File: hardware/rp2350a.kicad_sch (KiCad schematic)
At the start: 46 parts, among them Q2 DMN1150UFB-7B, Q3 DMN1150UFB-7B, U10 RP2354A, U11 TS2306A 240GF MSM 9_C2976675, X1 XTM25012000JT00351001

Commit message: piu1
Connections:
- net PIOUART0_RX: now also U10.5 (GPIO3); no longer U10.13 (GPIO9)
- net PIOUART0_TX: now also U10.4 (GPIO2); no longer U10.12 (GPIO8)
- net UART1_RX: now also U10.13 (GPIO9); no longer U10.5 (GPIO3)
- net UART1_TX: now also U10.12 (GPIO8); no longer U10.4 (GPIO2)
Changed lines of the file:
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@@
+		)
+	)
+	(hierarchical_label "UART1_TX"
+		(shape output)
+		(at 321.31 219.71 0)
+		(effects
+			(font
+				(size 1.27 1.27)
+			)
+			(justify left)
 		)
 	)
@@
 		)
 	)
-	(hierarchical_label "UART1_TX"
-		(shape output)
-		(at 321.31 226.06 0)
+	(hierarchical_label "PIOUART0_RX"
+		(shape input)
+		(at 321.31 228.6 0)
 		(effects
 			(font
@@
 		(shape output)
 		(at 321.31 264.16 0)
-		(effects
-			(font
-				(size 1.27 1.27)
-			)
-			(justify left)
-		)
-	)
-	(hierarchical_label "PIOUART0_RX"
-		(shape input)
-		(at 321.31 222.25 0)
 		(effects
 			(font
@@
 		)
 	)
-	(hierarchical_label "UART1_RX"
+	(hierarchical_label "UART0_RX"
 		(shape input)
-		(at 321.31 228.6 0)
+		(at 321.31 215.9 0)
 		(effects
 			(font
@@
 		)
 	)
-	(hierarchical_label "UART0_RX"
+	(hierarchical_label "UART1_RX"
 		(shape input)
-		(at 321.31 215.9 0)
+		(at 321.31 222.25 0)
 		(effects
 			(font
@@
 		)
 	)
-	(hierarchical_label "I2C0{SCL,SDA}"
-		(shape bidirectional)
-		(at 400.05 229.87 0)
+	(hierarchical_label "PIOUART0_TX"
+		(shape output)
+		(at 321.31 226.06 0)
 		(effects
 			(font
@@
 		)
 	)
-	(hierarchical_label "PIOUART0_TX"
-		(shape output)
-		(at 321.31 219.71 0)
+	(hierarchical_label "I2C0{SCL,SDA}"
+		(shape bidirectional)
+		(at 400.05 229.87 0)
 		(effects
 			(font

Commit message: switch spi
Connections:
- net BEEPER: now also U10.28 (GPIO17); no longer U10.9 (GPIO6)
- net FLASH_CS: now also U10.33 (GPIO21); no longer U10.17 (GPIO13)
- net GYRO_CS: now also U10.17 (GPIO13); no longer U10.33 (GPIO21)
- net GYRO_INT: now also U10.13 (GPIO9); no longer U10.28 (GPIO17)
- net I2C0.SCL: now also U10.8 (GPIO5); no longer U10.7 (GPIO4)
- net I2C0.SDA: now also U10.7 (GPIO4); no longer U10.8 (GPIO5)
- net LED_STRIP_L: now also U10.12 (GPIO8); no longer U10.10 (GPIO7)
- net UART1_RX: now also U10.10 (GPIO7); no longer U10.13 (GPIO9)
- net UART1_TX: now also U10.9 (GPIO6); no longer U10.12 (GPIO8)

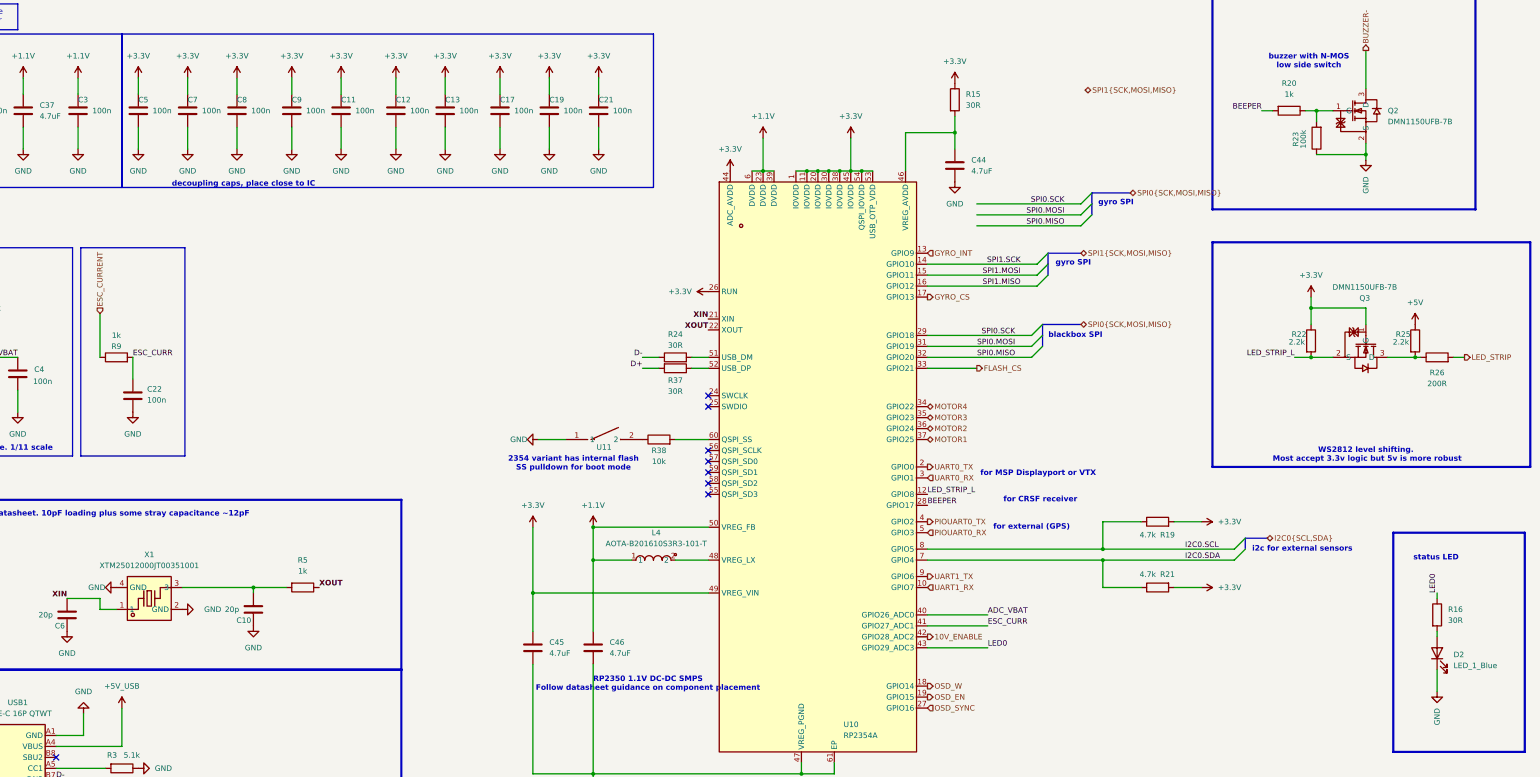
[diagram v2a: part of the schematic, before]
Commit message: some minor tweaks
- remove some unnecessary resistors
- slightly higher 10V rail to account for voltage drop
- some cleanup
- simpler PG 1.8V circuit
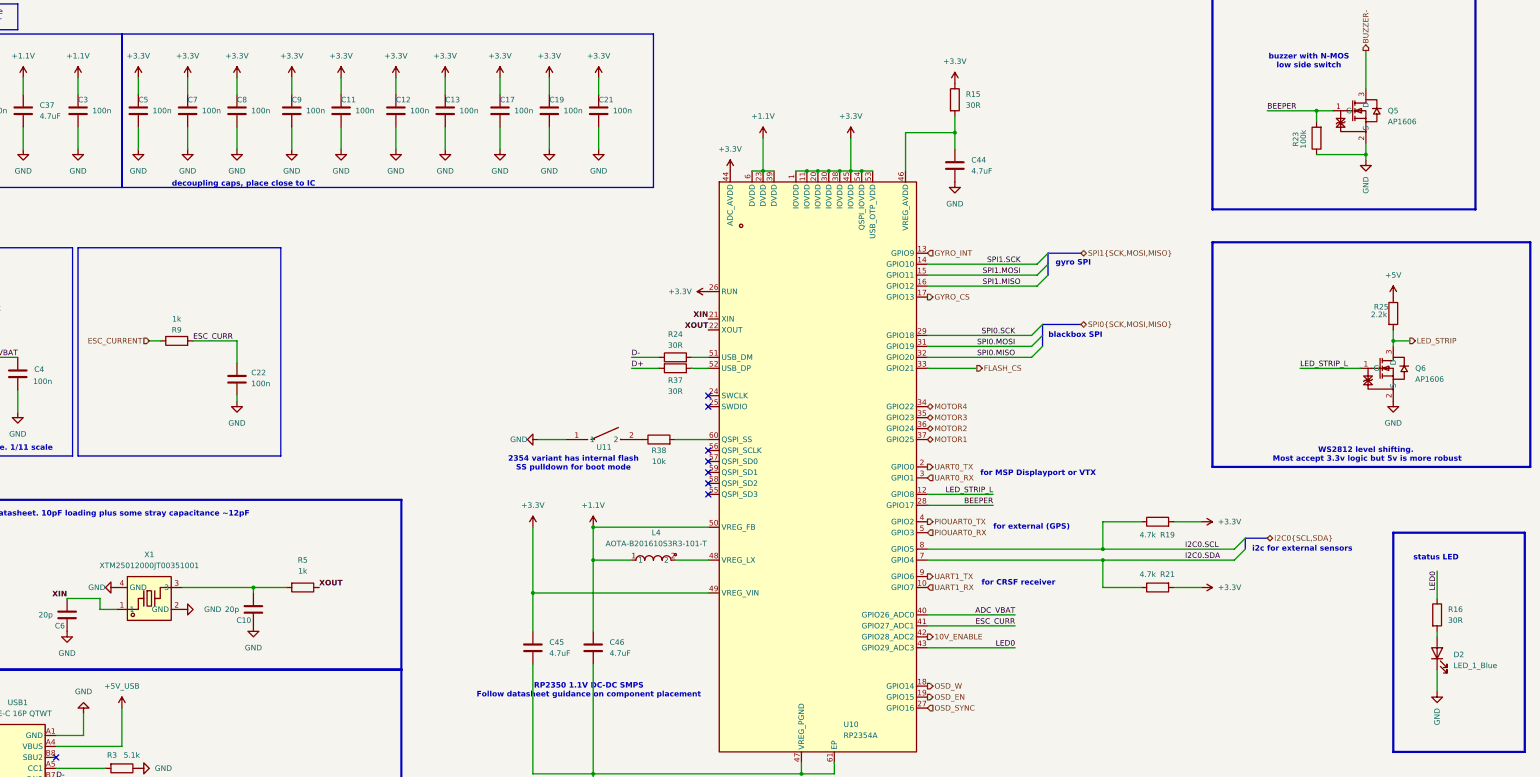
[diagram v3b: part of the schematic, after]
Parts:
- removed Q2, Q3: DMN1150UFB-7B, lib:DFN-3L_L1.0-W0.6-P0.65-BR, symbol lib:DMN1150UFB-7B
- removed R20: 1k, Resistor_SMD:R_0201_0603Metric, symbol Device:R
- removed R22: 2.2k, Resistor_SMD:R_0201_0603Metric, symbol Device:R
- removed R26: 200R, Resistor_SMD:R_0201_0603Metric, symbol Device:R
- added Q5, Q6: AP1606, lib:DFN-3L_L1.0-W0.6-P0.65-BR, symbol lib:DMN1150UFB-7B
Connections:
- net BEEPER: now also R23.2, Q5.1 (G)
- net BUZZER-: now also Q5.3 (D)
- net GND: now also Q5.2 (S), Q6.2 (S)
- net LED_STRIP: now also R25.2, Q6.3 (D)
- net LED_STRIP_L: now also Q6.1 (G)
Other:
- moved on the sheet: C22, R25, R9

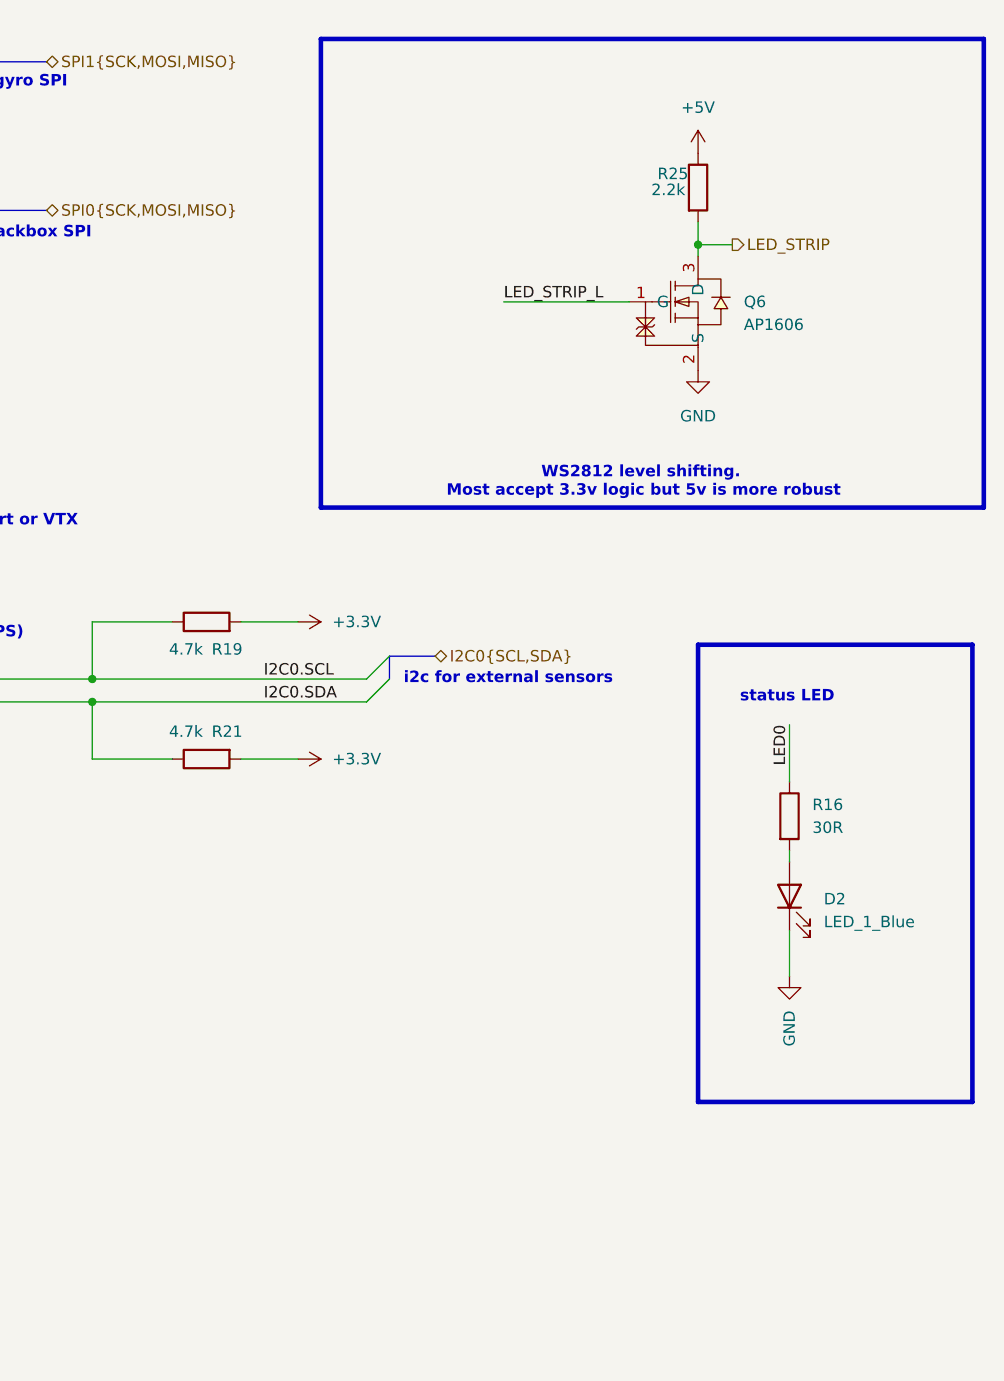
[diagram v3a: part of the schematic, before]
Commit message: LED resistors
Also reduced the amount of different resistors for cheaper assembly
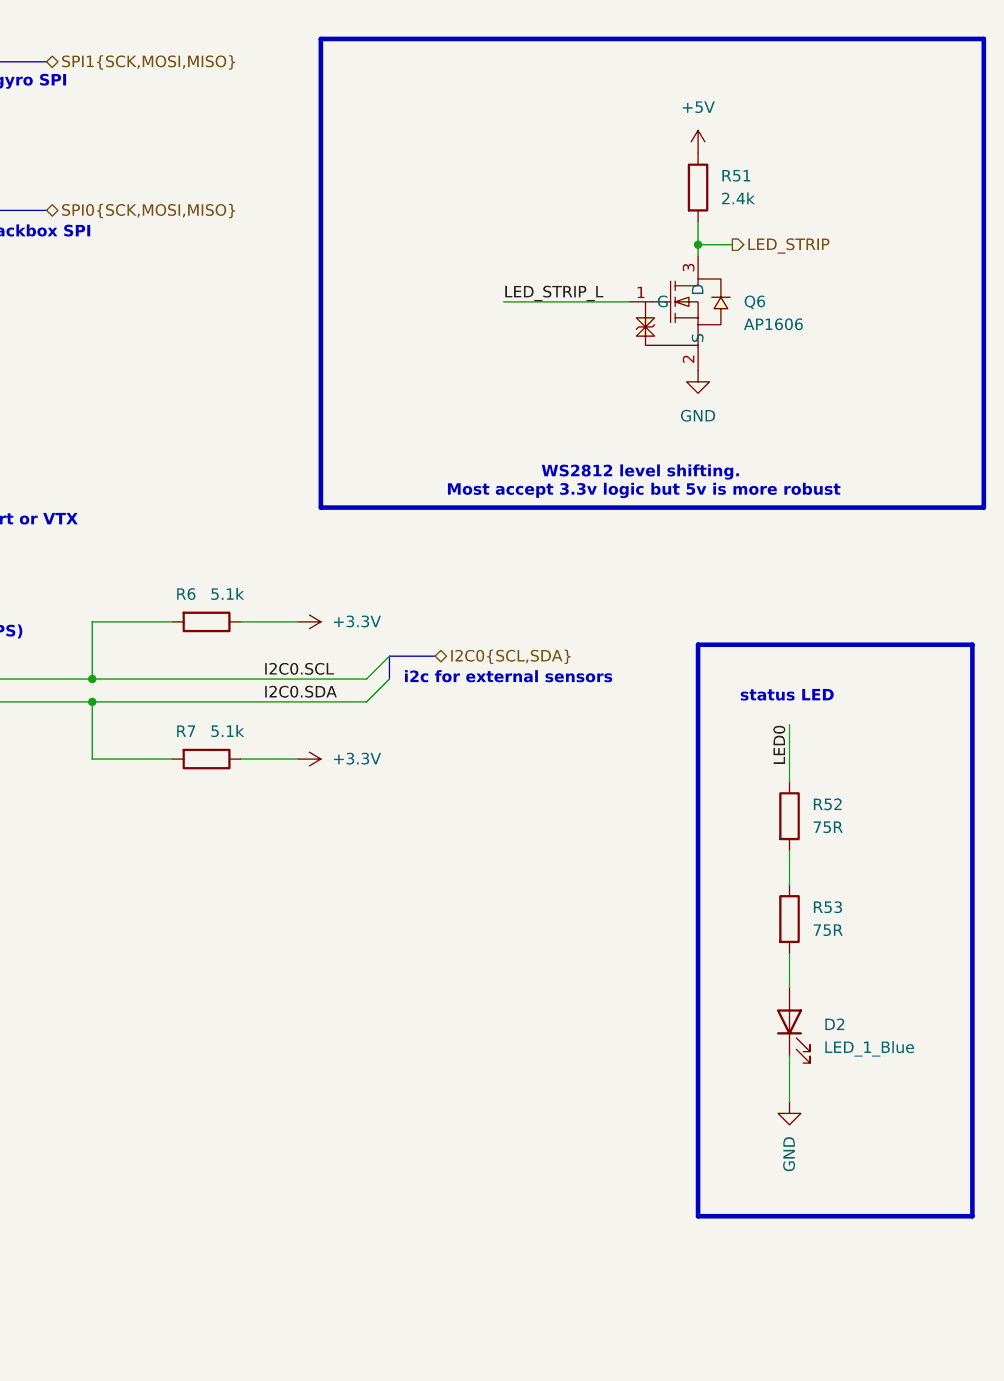
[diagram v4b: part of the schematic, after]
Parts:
- removed R16: 30R, Resistor_SMD:R_0201_0603Metric, symbol Device:R
- removed R19, R21: 4.7k, Resistor_SMD:R_0201_0603Metric, symbol Device:R
- removed R25: 2.2k, Resistor_SMD:R_0201_0603Metric, symbol Device:R
- added R51: 2.4k, Resistor_SMD:R_0201_0603Metric, symbol Device:R
- added R52, R53: 75R, Resistor_SMD:R_0201_0603Metric, symbol Device:R
- added R6, R7: 5.1k, Resistor_SMD:R_0201_0603Metric, symbol Device:R
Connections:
- net +3.3V: now also R6.1, R7.1
- net +5V: now also R51.1
- net I2C0.SCL: now also R6.2
- net I2C0.SDA: now also R7.2
- net LED0: now also R52.1
- net LED_STRIP: now also R51.2
- net at D2.2 (A): now also R53.2
- new net: R52.2, R53.1
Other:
- moved on the sheet: D2

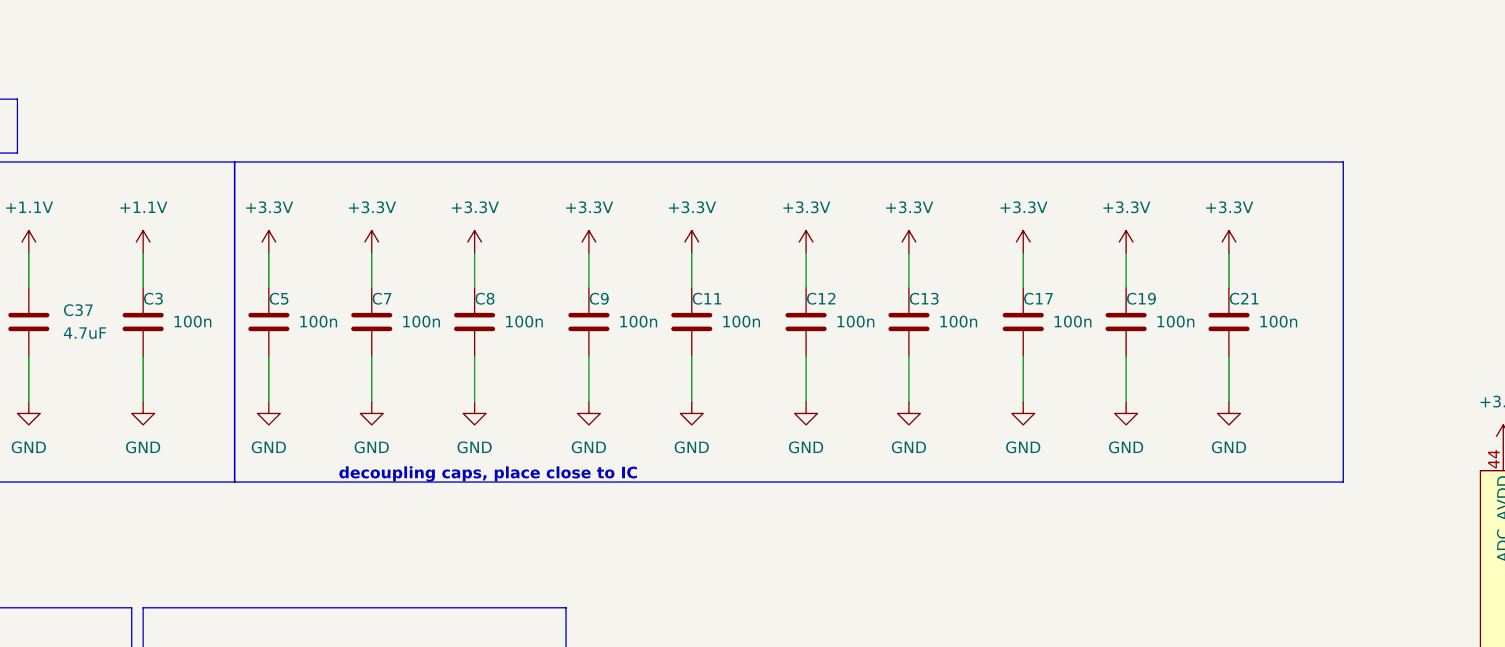
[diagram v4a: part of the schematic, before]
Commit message: remove some unneeded decoupling caps from RP2350
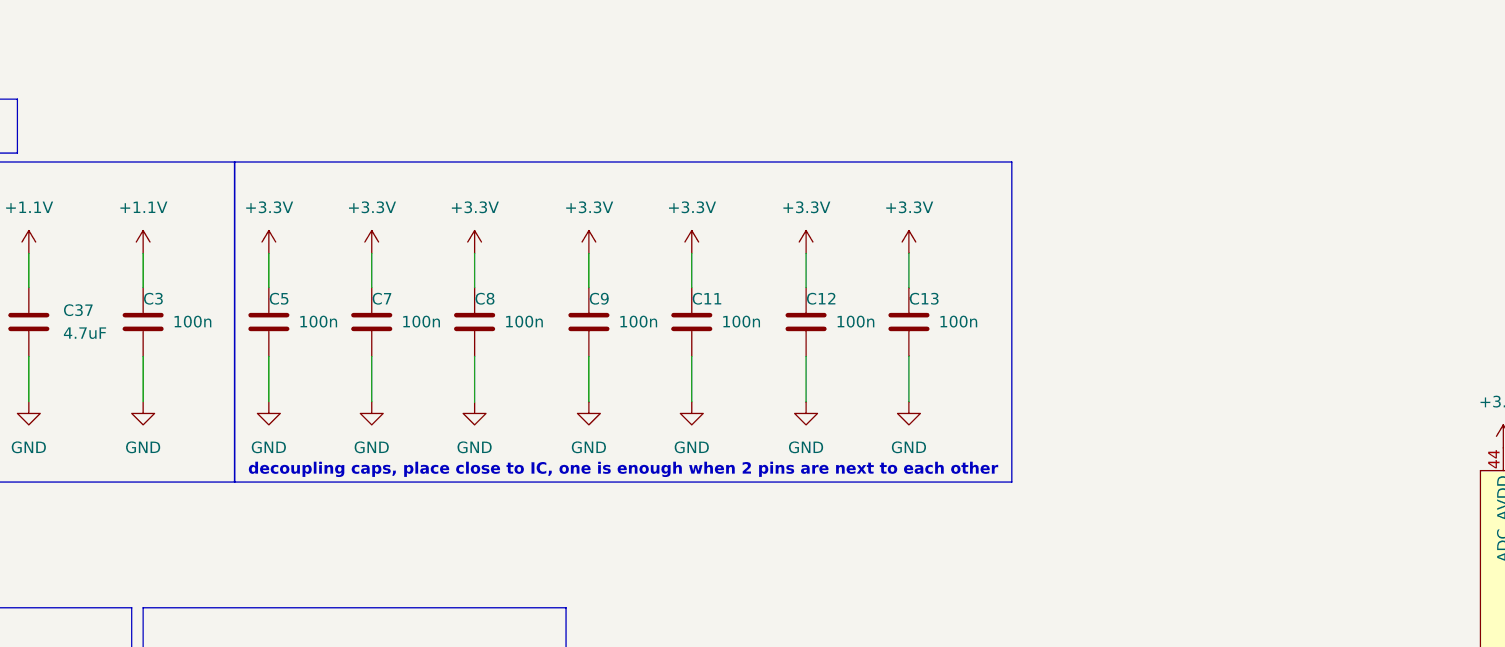
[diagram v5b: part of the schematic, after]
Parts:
- removed C17, C19, C21: 100n, Capacitor_SMD:C_0201_0603Metric, symbol Device:C
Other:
- note added: "decoupling caps, place close to IC, one is enough when 2 pins are next to each other"
- note removed: "decoupling caps, place close to IC"

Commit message: update MOSFET part numbers
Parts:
- Q5, Q6: LCSC Part C459538 -> C2849580
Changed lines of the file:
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@@
 			)
 		)
-		(property "LCSC Part" "C459538"
+		(property "LCSC Part" "C2849580"
 			(at 429.26 208.28 0)
 			(hide yes)
@@
 			)
 		)
-		(property "LCSC Part" "C459538"
+		(property "LCSC Part" "C2849580"
 			(at 422.91 148.59 0)
 			(hide yes)

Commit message: ROUTE
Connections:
- net 10V_ENABLE: now also U10.41 (GPIO27_ADC1); no longer U10.42 (GPIO28_ADC2)
- net ADC_VBAT: now also U10.43 (GPIO29_ADC3); no longer U10.40 (GPIO26_ADC0)
- net ESC_CURR: now also U10.42 (GPIO28_ADC2); no longer U10.41 (GPIO27_ADC1)
- net LED0: now also U10.40 (GPIO26_ADC0); no longer U10.43 (GPIO29_ADC3)
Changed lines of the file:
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@@
+	(wire
+		(pts
+			(xy 334.01 250.19) (xy 321.31 250.19)
+		)
+		(stroke
+			(width 0)
+			(type default)
+		)
+	)
 	(wire
 		(pts
@@
 	(wire
 		(pts
-			(xy 321.31 247.65) (xy 341.63 247.65)
-		)
-		(stroke
-			(width 0)
-			(type default)
-		)
-	)
-	(wire
-		(pts
 			(xy 283.21 137.16) (xy 283.21 144.78)
 		)
@@
 	(wire
 		(pts
-			(xy 321.31 250.19) (xy 341.63 250.19)
-		)
-		(stroke
-			(width 0)
-			(type default)
-		)
-	)
-	(wire
-		(pts
 			(xy 346.71 171.45) (xy 321.31 171.45)
 		)
@@
 		(pts
 			(xy 209.55 134.62) (xy 209.55 139.7)
-		)
-		(stroke
-			(width 0)
-			(type default)
-		)
-	)
-	(wire
-		(pts
-			(xy 321.31 255.27) (xy 341.63 255.27)
 		)
 		(stroke
@@
 	)
 	(label "ESC_CURR"
-		(at 341.63 250.19 180)
+		(at 321.31 252.73 0)
 		(effects
 			(font
@@
 				(thickness 0.1588)
 			)
-			(justify right bottom)
+			(justify left bottom)
 		)
 	)
@@
 	)
 	(label "LED0"
-		(at 341.63 255.27 180)
-		(effects
-			(font
-				(size 1.27 1.27)
-			)
-			(justify right bottom)
+		(at 321.31 247.65 0)
+		(effects
+			(font
+				(size 1.27 1.27)
+			)
+			(justify left bottom)
 		)
 	)
@@
 	)
 	(label "ADC_VBAT"
-		(at 341.63 247.65 180)
+		(at 321.31 255.27 0)
 		(effects
 			(font
@@
 				(thickness 0.1588)
 			)
-			(justify right bottom)
+			(justify left bottom)
 		)
 	)
@@
 	(hierarchical_label "10V_ENABLE"
 		(shape output)
-		(at 321.31 252.73 0)
-		(effects
-			(font
+		(at 334.01 250.19 0)
+		(effects
+			(font
